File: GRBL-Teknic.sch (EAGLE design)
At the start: 34 parts, among them U1 MIC5225-5.0YM5-TR, U2 ATmega328P-MU, U4 FT231XQ-x, X3 20329, Y2 CSTCE16M0V53-R0

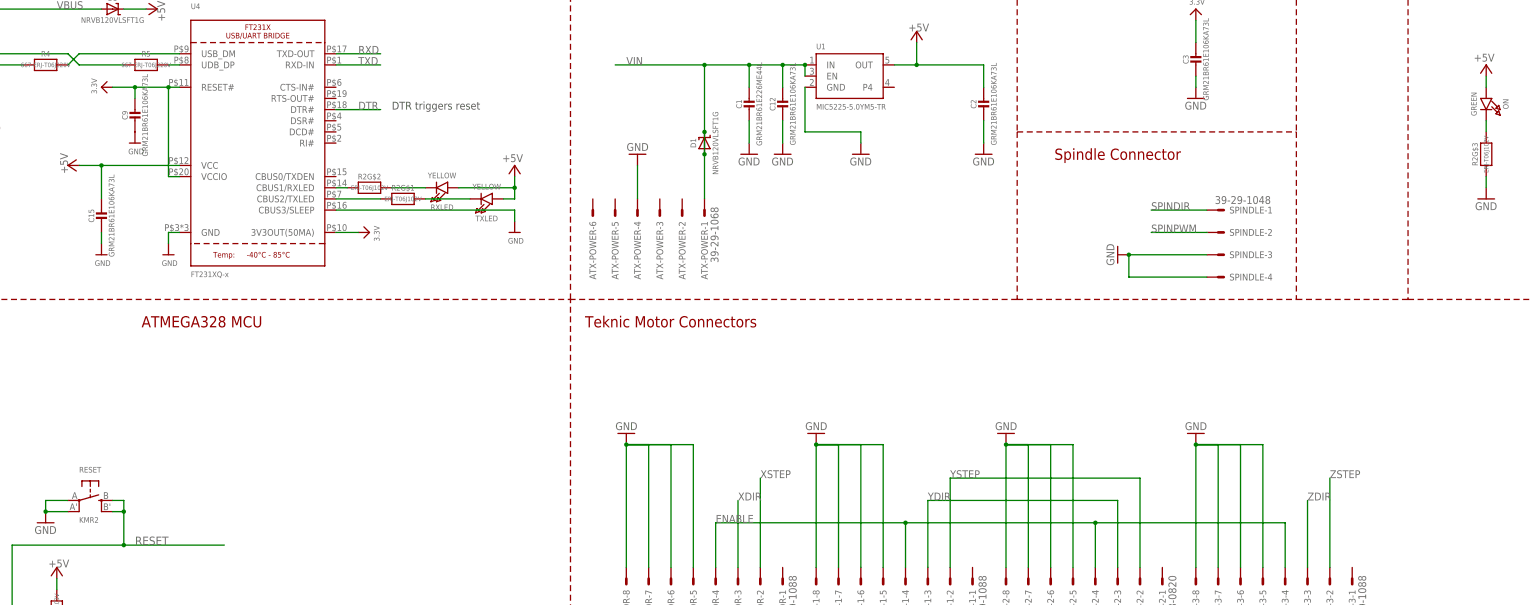
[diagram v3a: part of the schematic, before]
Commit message: fixes #4
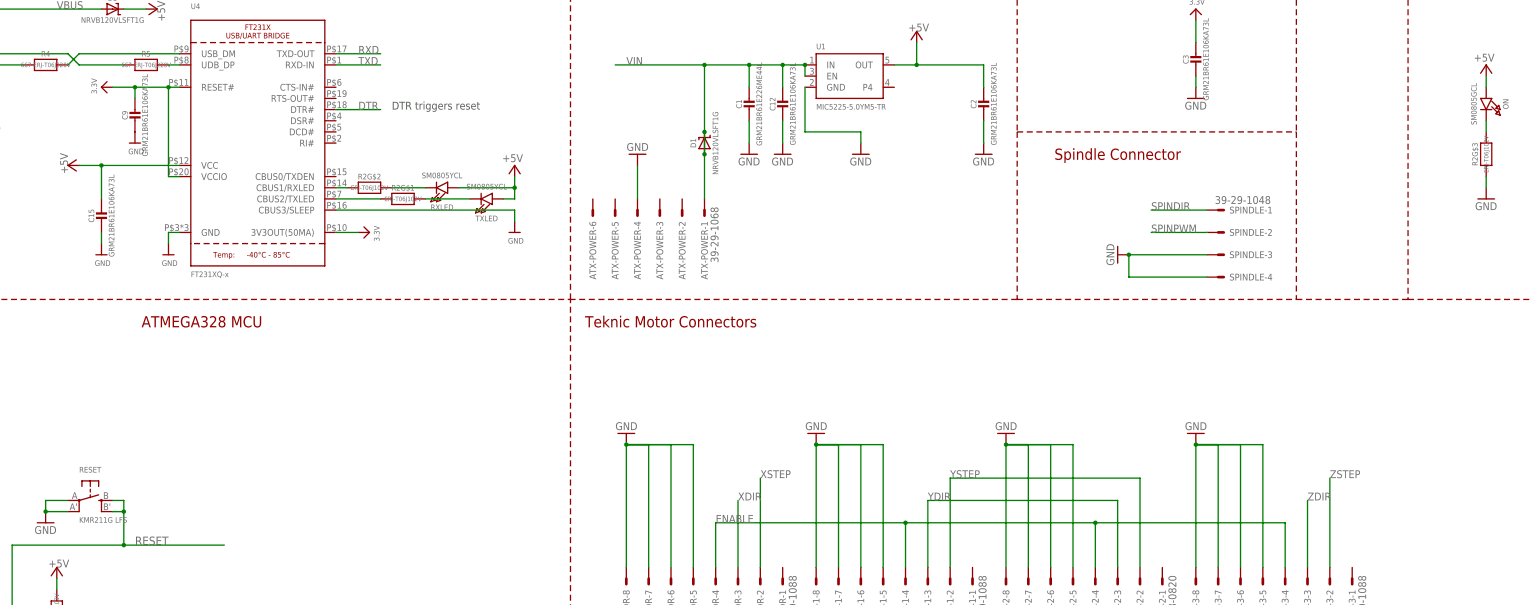
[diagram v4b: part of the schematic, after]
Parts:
- ON: value GREEN -> SM0805GCL
- RESET: value KMR2 -> KMR211G LFS
- RXLED, TXLED: value YELLOW -> SM0805YCL
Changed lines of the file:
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@@
 <part name="GND7" library="supply1" deviceset="GND" device=""/>
 <part name="GND12" library="supply1" deviceset="GND" device=""/>
-<part name="ON" library="microbuilder" deviceset="LED" device="0805_NOOUTLINE" value="GREEN"/>
+<part name="ON" library="microbuilder" deviceset="LED" device="0805_NOOUTLINE" value="SM0805GCL"/>
 <part name="GND14" library="supply1" deviceset="GND" device=""/>
 <part name="P+5" library="supply1" deviceset="+5V" device=""/>
@@
 <part name="P+14" library="supply1" deviceset="+5V" device=""/>
 <part name="X3" library="microbuilder" deviceset="USB_W_SHIELD" device="_20329" value="20329"/>
-<part name="TXLED" library="microbuilder" deviceset="LED" device="0805_NOOUTLINE" value="YELLOW"/>
-<part name="RXLED" library="microbuilder" deviceset="LED" device="0805_NOOUTLINE" value="YELLOW"/>
+<part name="TXLED" library="microbuilder" deviceset="LED" device="0805_NOOUTLINE" value="SM0805YCL"/>
+<part name="RXLED" library="microbuilder" deviceset="LED" device="0805_NOOUTLINE" value="SM0805YCL"/>
 <part name="U$13" library="microbuilder" deviceset="GND" device=""/>
 <part name="U$21" library="microbuilder" deviceset="GND" device=""/>
@@
 <part name="U$6" library="microbuilder" deviceset="GND" device=""/>
 <part name="P+7" library="supply1" deviceset="+5V" device=""/>
-<part name="RESET" library="microbuilder" deviceset="SWITCH_TACT_SMT" device="4.6X2.8" value="KMR2"/>
+<part name="RESET" library="microbuilder" deviceset="SWITCH_TACT_SMT" device="4.6X2.8" value="KMR211G LFS"/>
 <part name="R8" library="microbuilder" deviceset="RESISTOR" device="0805_NOOUTLINE" value="ERJ-T06J103V"/>
 <part name="R11" library="microbuilder" deviceset="RESISTOR" device="0805_NOOUTLINE" value="ERJ-T06J102V"/>

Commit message: ready to try sample order
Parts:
- removed ATX-POWER: 39-29-1068, con-molex-2:555X-6H
- removed C1: GRM21BR61E226ME44L, microbuilder:CAP_CERAMIC0805-NOOUTLINE
- removed C10, C6: GRM21BR71E104KA01L, microbuilder:CAP_CERAMIC0805-NOOUTLINE
- removed C12, C15, C2, C3, C9: GRM21BR61E106KA73L, microbuilder:CAP_CERAMIC0805-NOOUTLINE
- removed C5: GRM21BR71E104KA01L, microbuilder:CAP_CERAMIC_0805MP
- removed D1, D3: NRVB120VLSFT1G, microbuilder:DIODE-SCHOTTKYSOD-123
- removed ON: SM0805GCL, microbuilder:LED0805_NOOUTLINE
- removed R11: ERJ-T06J102V, microbuilder:RESISTOR0805_NOOUTLINE
- removed R2: ERJ-T06J102V, microbuilder:RESISTOR_4PACK
- removed R4: 667-ERJ-T06J220V, microbuilder:RESISTOR0805_NOOUTLINE
- removed R5: 667-ERJ-T06J220V, microbuilder:RESISTOR_0805MP
- removed R8: ERJ-T06J103V, microbuilder:RESISTOR0805_NOOUTLINE
- removed RESET: KMR211G LFS, microbuilder:SWITCH_TACT_SMT4.6X2.8
- removed RXLED, TXLED: SM0805YCL, microbuilder:LED0805_NOOUTLINE
- removed SPINDLE: 39-29-1048, con-molex-2:555X-4H
- removed U1: MIC5225-5.0YM5-TR, microbuilder:VREG_SOT23-5
- removed U2: ATmega328P-MU, microbuilder:ATMEGA328P
- removed U4: FT231XQ-x, microbuilder:FT231X
- removed X-LIMIT, Y-LIMIT, Z-LIMIT: 39-29-1088, con-molex-2:555X-2H
- removed X-MOTOR, Y-MOTOR-1, Y-MOTOR-3: 39-29-1088, con-molex-2:555X-8H
- removed X3: 20329, microbuilder:USB_W_SHIELD_20329
- removed Y-MOTOR-2: 35318-0820, con-molex-2:555X-8H
- removed Y2: CSTCE16M0V53-R0, SmartPrj:RESONATORMU
- added B1: ARDUINO_UNO_R3_SHIELDBASIC, SparkFun-Boards:ARDUINO_UNO_R3_SHIELDBASIC
- added LIMX+, LIMY+, LIMZ+: (no value), con-molex-2:555X-2V
- added MOTORX, MOTORY, MOTORZ: (no value), con-molex-2:555X-8V
- added TOOL: (no value), con-molex-2:555X-6V
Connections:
- removed net +5V: C10.2, C15.1, C2.1, C6.2, D3.C, ON.A, R8.2, RXLED.A, TXLED.A, U1.OUT, U2.AVCC, U2.VCC, U4.VCC
- removed net 3.3V: C3.1, C9.1, U4.3V3OUT(50MA), U4.RESET#, U4.VCCIO
- removed net ABORT: U2.(ADC0)PC0
- removed net AREF: U2.AREF
- removed net COOLANT: U2.(ADC3)PC3
- removed net D+: R5.1, X3CONN.D+
- removed net D-: R4.1, X3CONN.D-
- removed net DTR: C5.1, U4.DTR#
- removed net ENABLE: U2.(ICP)PB0, X-MOTOR-4.S, Y-MOTOR-1-4.S, Y-MOTOR-2-4.S, Y-MOTOR-3-4.S
- removed net HOLD: U2.(ADC1)PC1
- removed net IO0: R11.1, U2.(RXD)PD0
- removed net N$10: R5.2, U4.UDB_DP
- removed net N$3: ON.C, R2G$3.2
- removed net N$4: R2G$2.1, U4.CBUS1/RXLED
- removed net N$5: R2G$2.2, RXLED.C
- removed net N$7: R2G$1.2, TXLED.C
- removed net N$9: R4.2, U4.USB_DM
- removed net PROBE: U2.(ADC5)PC5
- removed net RESERVED: U2.(ADC4)PC4
- removed net RESET: C5.2, R8.1, RESET.S, RESET.S1, U2.RESET
- removed net RXD: R11.2, U4.TXD-OUT
- removed net START: U2.(ADC2)PC2
- removed net TXD: U2.(TXD)PD1, U4.RXD-IN
- removed net VBUS: D3.A, X3CONN.VBUS
- removed net XDIR: U2.(T1)PD5, X-MOTOR-3.S
- removed net XLIM: U2.(OC1)PB1, X-LIMIT-1.S
- removed net XSTEP: U2.(INT0)PD2, X-MOTOR-2.S
- removed net XTAL1: U2.XTAL1, Y2.3
- removed net XTAL2: U2.XTAL2, Y2.1
- removed net YDIR: U2.(AIN0)PD6, Y-MOTOR-1-3.S, Y-MOTOR-2-3.S
- removed net YLIM: U2.(SS)PB2, Y-LIMIT-1.S
- removed net YSTEP: U2.(INT1)PD3, Y-MOTOR-1-2.S, Y-MOTOR-2-2.S
- removed net ZDIR: U2.(AIN1)PD7, Y-MOTOR-3-3.S
- removed net ZLIM: U2.(MISO)PB4, Z-LIMIT-1.S
- removed net ZSTEP: U2.(TO)PD4, Y-MOTOR-3-2.S
- new net DIRX: B1.*D5, MOTORX-3.S
- new net DIRY: B1.*D6, MOTORY-3.S
- new net DIRZ: B1.D8, MOTORX-4.S, MOTORY-4.S, MOTORZ-4.S
- new net LIMX: B1.*D9, LIMX+-1.S
- new net LIMY: B1.*D10, LIMY+-1.S
- new net LIMZ: B1.D12, LIMZ+-1.S
- new net STEPX: B1.D2, MOTORX-2.S
- new net STEPY: B1.*D3, MOTORY-2.S
- new net STEPZ: B1.D4, MOTORZ-2.S
- net GND: now also B1.GND@0, LIMX+-2.S, LIMY+-2.S, LIMZ+-2.S, MOTORX-5.S, MOTORX-6.S, MOTORX-7.S, MOTORX-8.S, MOTORY-5.S, MOTORY-6.S, MOTORY-7.S, MOTORY-8.S, MOTORZ-5.S, MOTORZ-6.S, MOTORZ-7.S, MOTORZ-8.S, TOOL-4.S, TOOL-5.S, TOOL-6.S; no longer ATX-POWER-4.S, C1.2, C10.1, C12.2, C15.2, C2.2, C3.2, C6.1, C9.2, R2G$3.1, RESET.P, RESET.P1, SPINDLE-3.S, SPINDLE-4.S, U1.GND, U2.AGND, U2.GND, U4.CBUS3/SLEEP, U4.GND, X-LIMIT-2.S, X-MOTOR-5.S, X-MOTOR-6.S, X-MOTOR-7.S, X-MOTOR-8.S, X3CONN.GND, X3SHIELD.1, Y-LIMIT-2.S, Y-MOTOR-1-5.S, Y-MOTOR-1-6.S, Y-MOTOR-1-7.S, Y-MOTOR-1-8.S, Y-MOTOR-2-5.S, Y-MOTOR-2-6.S, Y-MOTOR-2-7.S, Y-MOTOR-2-8.S, Y-MOTOR-3-5.S, Y-MOTOR-3-6.S, Y-MOTOR-3-7.S, Y-MOTOR-3-8.S, Y2.2, Z-LIMIT-2.S
- net N$6: now also B1.D7, MOTORZ-3.S; no longer R2G$1.1, U4.CBUS2/TXLED
- net SPINDIR: now also B1.D13, TOOL-2.S; no longer SPINDLE-1.S, U2.(SCK)PB5
- net SPINPWM: now also B1.*D11, TOOL-3.S; no longer SPINDLE-2.S, U2.(MOSI)PB3
- net VIN: now also B1.VIN, TOOL-1.S; no longer ATX-POWER-1.S, C1.1, C12.1, D1.A, D1.C, U1.EN, U1.IN
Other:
- note removed: "ATMEGA328 MCU"
- note removed: "DTR triggers reset"
- note removed: "Limit Connectors"
- note removed: "POWER LED"
- note removed: "POWER SUPPLY: 12V ATX -> 5V"
- note removed: "POWER SUPPLY: 3.3V"
- note removed: "Spindle Connector"
- note removed: "Teknic Motor Connectors"
- note removed: "USB/Serial Bridge"

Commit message: updated with coolant connection
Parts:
- added COOL: (no value), con-molex-2:555X-2V
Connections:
- new net COOL: B1.A3, COOL-1.S
- net GND: now also B1.GND@1, COOL-2.S
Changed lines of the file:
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@@
 <part name="LIMZ+" library="con-molex-2" deviceset="555X-2" device="V"/>
 <part name="TOOL" library="con-molex-2" deviceset="555X-6" device="V"/>
+<part name="COOL" library="con-molex-2" deviceset="555X-2" device="V"/>
 </parts>
 <sheets>
@@
 <instance part="TOOL" gate="-5" x="22.86" y="-10.16" rot="R270"/>
 <instance part="TOOL" gate="-6" x="17.78" y="-10.16" rot="R270"/>
+<instance part="COOL" gate="-1" x="5.08" y="-10.16" rot="R270"/>
+<instance part="COOL" gate="-2" x="0" y="-10.16" rot="R270"/>
 </instances>
 <busses>
@@
 <wire x1="17.78" y1="25.4" x2="12.7" y2="25.4" width="0.1524" layer="91"/>
 <label x="10.16" y="25.4" size="1.778" layer="95"/>
+<wire x1="12.7" y1="25.4" x2="12.7" y2="27.94" width="0.1524" layer="91"/>
+<pinref part="B1" gate="G$1" pin="GND@1"/>
+<wire x1="12.7" y1="27.94" x2="17.78" y2="27.94" width="0.1524" layer="91"/>
 </segment>
 <segment>
@@
 </segment>
 <segment>
-<wire x1="17.78" y1="27.94" x2="12.7" y2="27.94" width="0.1524" layer="91"/>
-<label x="10.16" y="27.94" size="1.778" layer="95"/>
+<wire x1="0" y1="-7.62" x2="0" y2="-2.54" width="0.1524" layer="91"/>
+<label x="0" y="-2.54" size="1.778" layer="95"/>
+<pinref part="COOL" gate="-2" pin="S"/>
 </segment>
 </net>
@@
 </segment>
 </net>
+<net name="COOL" class="0">
+<segment>
+<pinref part="COOL" gate="-1" pin="S"/>
+<wire x1="5.08" y1="-7.62" x2="5.08" y2="58.42" width="0.1524" layer="91"/>
+<pinref part="B1" gate="G$1" pin="A3"/>
+<wire x1="5.08" y1="58.42" x2="17.78" y2="58.42" width="0.1524" layer="91"/>
+</segment>
+</net>
